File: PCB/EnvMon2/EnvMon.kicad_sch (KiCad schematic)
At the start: 40 parts, among them J1 USB-C, J2 DC, J3 TEMP, J4 Shelly, M1 OLED1.5-RGB, SW1 SW_Push, SW2 SW_Push, SW3 SW_Push, U1 LMR16006XDDCR, U2 SCD41, U3 FT231XQ, U4 ESP32-PICO-MINI-02, U5 QR, U7 SHT40, U8 VEML6040

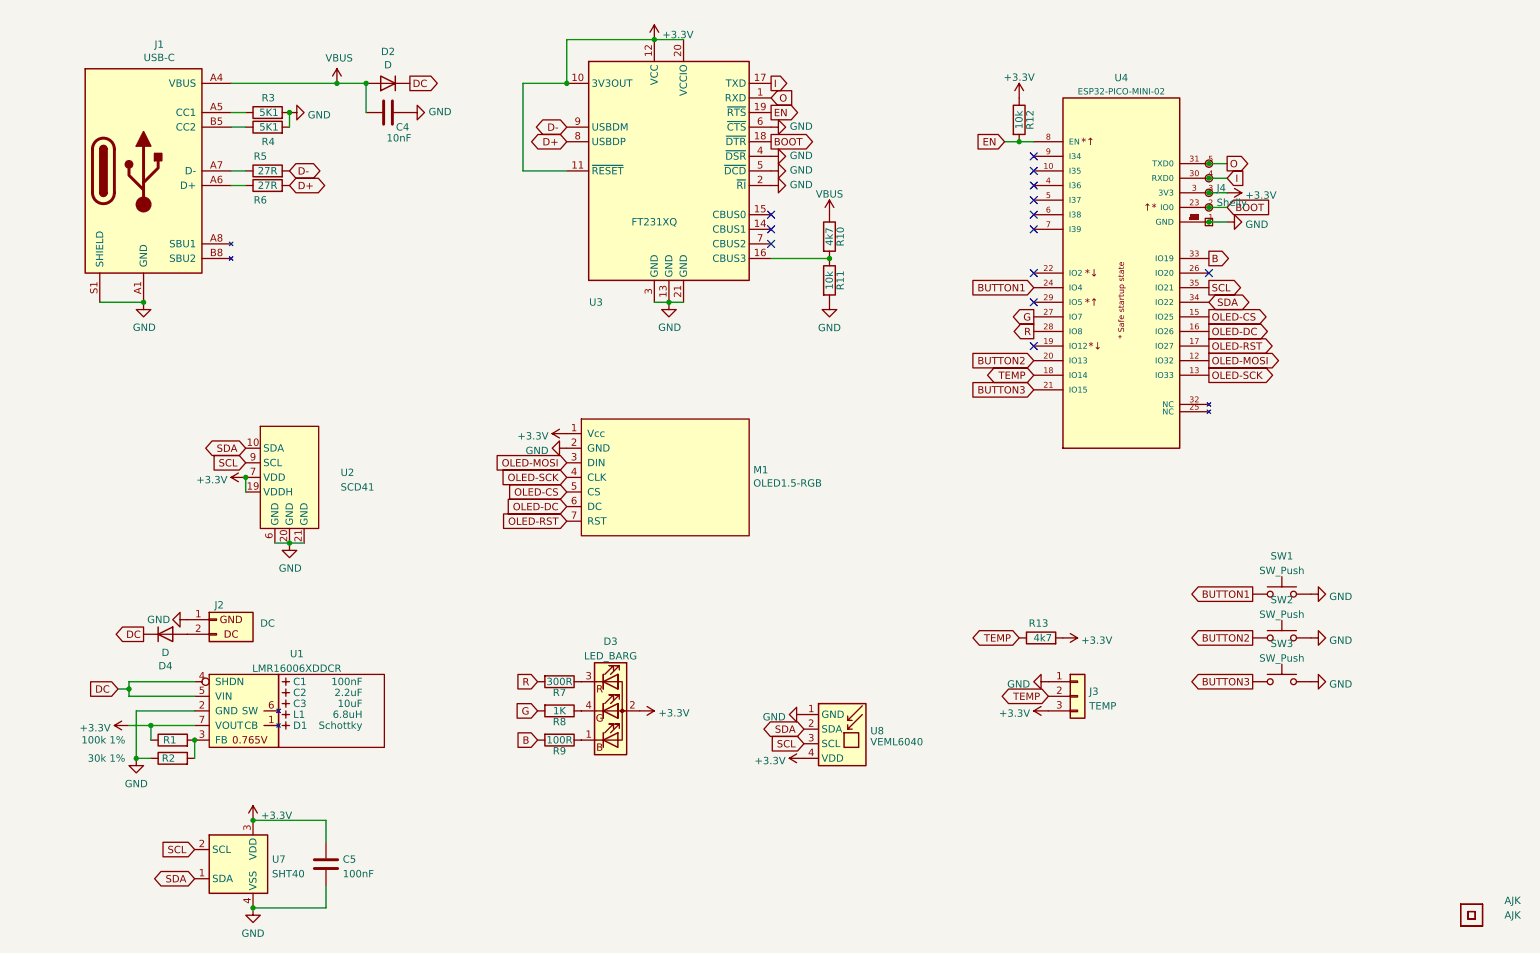
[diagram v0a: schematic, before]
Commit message: S3 board basic tracking started
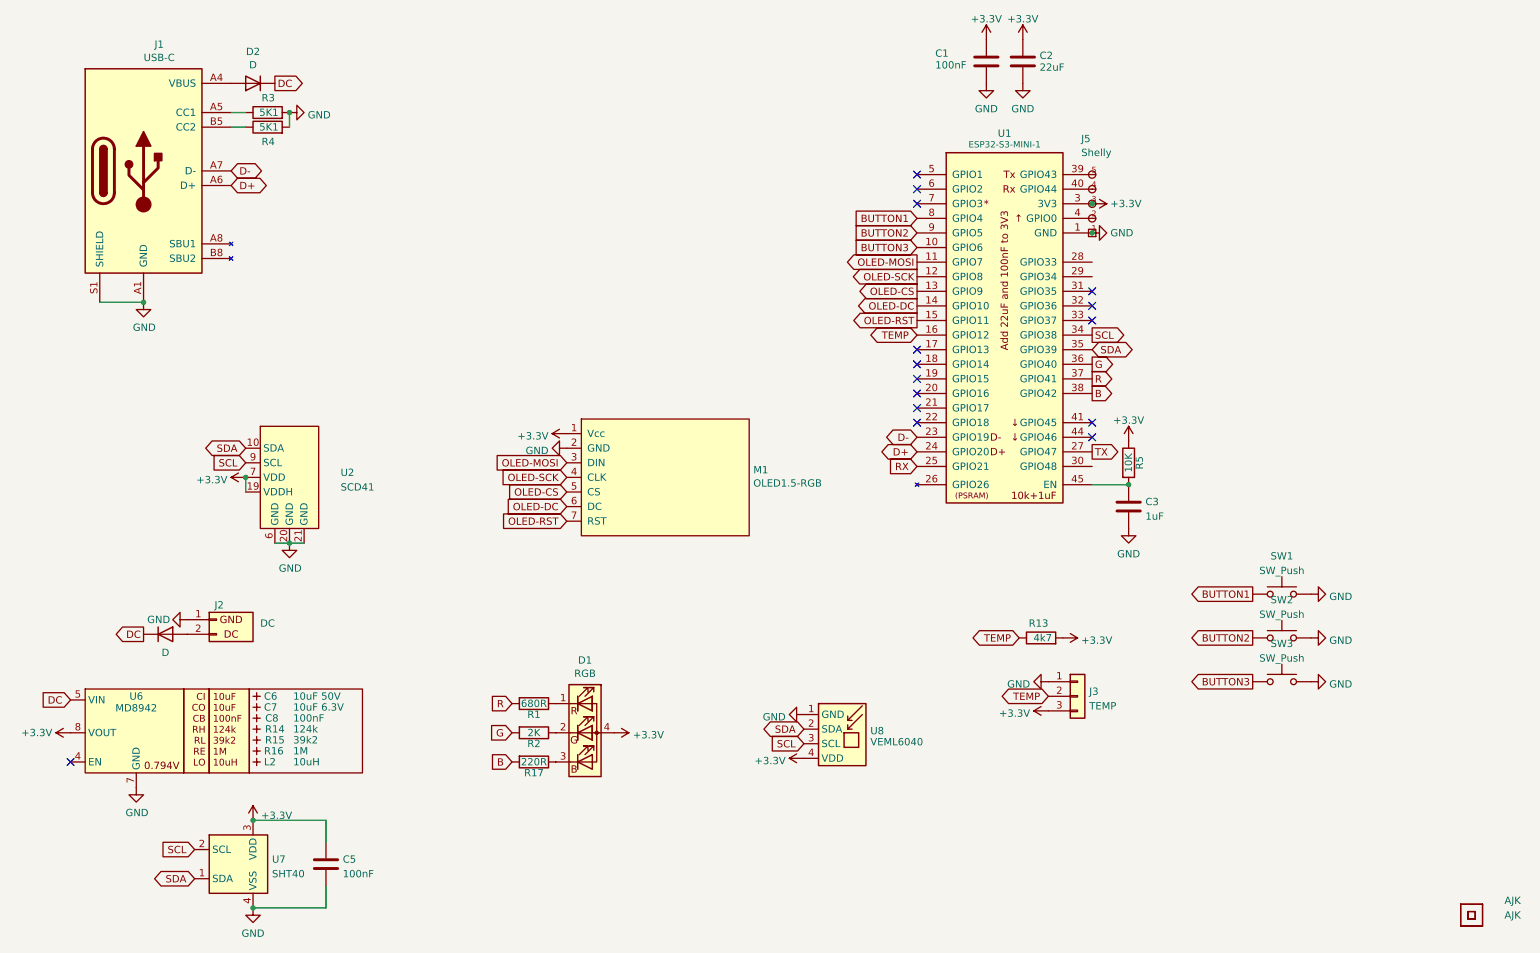
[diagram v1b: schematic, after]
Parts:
- removed C1: 100nF, RevK:C_0603_, symbol RevK:Hidden
- removed C2: 2.2uF, RevK:C_0805_, symbol RevK:Hidden
- removed C3: 10uF, RevK:C_0805_, symbol RevK:Hidden
- removed C4: 10nF, RevK:C_0603, symbol Device:C
- removed D1: Schottky, RevK:D_1206_, symbol RevK:Hidden
- removed D3: LED_BARG, RevK:MHS190RGBCT, symbol Device:LED_BARG
- removed J4: Shelly, RevK:Shelly, symbol RevK:Shelly
- removed L1: 6.8uH, RevK:L_4x4_, symbol RevK:Hidden
- removed R10: 4k7, RevK:R_0603, symbol Device:R
- removed R11, R12: 10k, RevK:R_0603, symbol Device:R
- removed R6: 27R, RevK:R_0603, symbol Device:R
- removed R7: 300R, RevK:R_0603, symbol Device:R
- removed R8: 1K, RevK:R_0603, symbol Device:R
- removed R9: 100R, RevK:R_0603, symbol Device:R
- removed U1: LMR16006XDDCR, RevK:SOT-23-Thin-6-Reg, symbol RevK:LMR16006XDDCR
- removed U3: FT231XQ, RevK:QFN-20-1EP_4x4mm_P0.5mm_EP2.5x2.5mm, symbol RevK:FT231XQ
- removed U4: ESP32-PICO-MINI-02, RevK:ESP32-PICO-MINI-02, symbol RevK:ESP32-PICO-MINI-02
- added C1: 100nF, RevK:C_0402, symbol Device:C
- added C2: 22uF, RevK:C_0402, symbol Device:C
- added C3: 1uF, RevK:C_0402, symbol Device:C
- added C6: 10uF 50V, RevK:C_0603_, symbol RevK:Hidden
- added C7: 10uF 6.3V, RevK:C_0603_, symbol RevK:Hidden
- added C8: 100nF, RevK:C_0603_, symbol RevK:Hidden
- added D1: RGB, RevK:LED-RGB-1.6x1.6, symbol Device:LED_RGBA
- added J5: Shelly, RevK:Shelly, symbol RevK:Shelly
- added L2: 10uH, RevK:L_4x4_, symbol RevK:Hidden
- added R14: 124k, RevK:R_0402_, symbol RevK:Hidden
- added R15: 39k2, RevK:R_0402_, symbol RevK:Hidden
- added R16: 1M, RevK:R_0402_, symbol RevK:Hidden
- added R17: 220R, RevK:R_0402, symbol Device:R
- added U1: ESP32-S3-MINI-1, RevK:ESP32-S3-MINI-1, symbol RevK:ESP32-S3-MINI-1-N4R2
- added U6: MD8942, RevK:SOT-23-6-MD8942, symbol RevK:MD89420-RegBlock
- C5: footprint RevK:C_0603 -> RevK:C_0402
- R1: value 100k 1% -> 680R; footprint RevK:R_0603 -> RevK:R_0402; LCSC Part # C14675 -> (none)
- R13, R3, R4: footprint RevK:R_0603 -> RevK:R_0402
- R2: value 30k 1% -> 2K; footprint RevK:R_0603 -> RevK:R_0402; LCSC Part # C100001 -> (none)
- R5: value 27R -> 10K; footprint RevK:R_0603 -> RevK:R_0402
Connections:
- net +3.3V: now also R5.1, C1.1, C2.1, D1.4 (A), J5.3 (3V3), U1.3 (3V3), U6.8 (VOUT); no longer R1.1
- net B: now also R17.2, U1.38 (GPIO42)
- net BUTTON1: now also U1.8 (GPIO4)
- net BUTTON2: now also U1.9 (GPIO5)
- net BUTTON3: now also U1.10 (GPIO6)
- net D+: now also J1.A6 (D+), J1.B6 (D+), U1.24 (GPIO20)
- net D-: now also J1.A7 (D-), J1.B7 (D-), U1.23 (GPIO19); no longer R5.2
- net DC: now also U6.5 (VIN)
- net G: now also R2.2, U1.36 (GPIO40)
- net GND: now also C1.2, C2.2, C3.2, J5.1 (GND), U1.1 (GND), U1.2 (GND), U1.42 (GND), U1.43 (GND), U1.46 (GND), U1.47 (GND), U1.48 (GND), U1.49 (GND), U1.50 (GND), U1.51 (GND), U1.52 (GND), U1.53 (GND), U1.54 (GND), U1.55 (GND), U1.56 (GND), U1.57 (GND), U1.58 (GND), U1.59 (GND), U1.60 (GND), U1.61 (GND), U1.62 (GND), U1.63 (GND), U1.64 (GND), U1.65 (GND), U6.2 (GND), U6.7 (GND); no longer R2.1
- net OLED-CS: now also U1.13 (GPIO9)
- net OLED-DC: now also U1.14 (GPIO10)
- net OLED-MOSI: now also U1.11 (GPIO7)
- net OLED-RST: now also U1.15 (GPIO11)
- net OLED-SCK: now also U1.12 (GPIO8)
- net R: now also R1.2, U1.37 (GPIO41)
- net SCL: now also U1.34 (GPIO38)
- net SDA: now also U1.35 (GPIO39)
- net TEMP: now also U1.16 (GPIO12)
- net VBUS: no longer names the net of D2.2 (A), J1.A4 (VBUS), J1.A9 (VBUS), J1.B4 (VBUS), J1.B9 (VBUS)
- new net: J5.2 (0), U1.4 (GPIO0)
- new net: J5.4 (Rx), U1.40 (GPIO44)
- new net: J5.5 (Tx), U1.39 (GPIO43)
- new net: D1.2 (GK), R2.1
- new net: C3.1, R5.2, U1.45 (EN)
- new net: D1.1 (RK), R1.1
- new net: D1.3 (BK), R17.1
- new net RX: U1.25 (GPIO21)
- new net TX: U1.27 (GPIO47)
- no-connect marks 13 -> 15
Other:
- moved on the sheet: D2

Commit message: Pretty tracks
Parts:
- removed D4: D, RevK:D_1206, symbol Device:D
- added D3: D, RevK:D_SOD-123, symbol Device:D
- D2: footprint RevK:D_1206 -> RevK:D_SOD-123; LCSC Part # C143805 -> C1884542
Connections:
- net DC: now also D3.1 (K)
- net at J1.A4 (VBUS), J1.A9 (VBUS), J1.B4 (VBUS)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: now also D3.2 (A); no longer D2.2 (A)
- net at J2.2 (DC): now also D2.2 (A)
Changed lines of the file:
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@@
+    )
+  )
+  (symbol (lib_id "Device:D") (at 44.45 123.825 0) (unit 1)
+    (in_bom yes) (on_board yes) (dnp no)
+    (property "Reference" "D2" (at 44.45 129.3368 0)
+      (effects (font (size 1.27 1.27)))
+    )
+    (property "Value" "D" (at 44.45 127.0254 0)
+      (effects (font (size 1.27 1.27)))
+    )
+    (property "Footprint" "RevK:D_SOD-123" (at 44.45 123.825 0)
+      (effects (font (size 1.27 1.27)) hide)
+    )
+    (property "Datasheet" "~" (at 44.45 123.825 0)
+      (effects (font (size 1.27 1.27)) hide)
+    )
+    (property "LCSC Part #" "C1884542" (at 44.45 123.825 0)
+      (effects (font (size 1.27 1.27)) hide)
+    )
+    (pin "1")
+    (pin "2")
+    (instances
+      (project "EnvMon"
+        (path "/12422a89-3d0c-485c-9386-f77121fd68fd"
+          (reference "D2") (unit 1)
+        )
+      )
+      (project "Access"
+        (path "/2a267270-6585-45e3-a633-b53049f10066"
+          (reference "D8") (unit 1)
+        )
+      )
+      (project "GenericS3"
+        (path "/2d210a96-f81f-42a9-8bf4-1b43c11086f3"
+          (reference "D1") (unit 1)
+        )
+      )
     )
   )
@@
     )
   )
-  (symbol (lib_id "Device:D") (at 44.45 123.825 0) (unit 1)
-    (in_bom yes) (on_board yes) (dnp no)
-    (property "Reference" "D4" (at 44.45 129.3368 0)
-      (effects (font (size 1.27 1.27)) hide)
-    )
-    (property "Value" "D" (at 44.45 127.0254 0)
-      (effects (font (size 1.27 1.27)))
-    )
-    (property "Footprint" "RevK:D_1206" (at 44.45 123.825 0)
-      (effects (font (size 1.27 1.27)) hide)
-    )
-    (property "Datasheet" "~" (at 44.45 123.825 0)
-      (effects (font (size 1.27 1.27)) hide)
-    )
-    (property "LCSC Part #" "C143805" (at 44.45 123.825 0)
-      (effects (font (size 1.27 1.27)) hide)
-    )
-    (pin "1")
-    (pin "2")
-    (instances
-      (project "EnvMon"
-        (path "/12422a89-3d0c-485c-9386-f77121fd68fd"
-          (reference "D4") (unit 1)
-        )
-      )
-    )
-  )
   (symbol (lib_id "Device:R") (at 196.85 124.46 90) (unit 1)
     (in_bom yes) (on_board yes) (dnp no)
@@
         (path "/12422a89-3d0c-485c-9386-f77121fd68fd"
           (reference "U5") (unit 1)
+        )
+      )
+    )
+  )
+  (symbol (lib_id "Device:D") (at 59.69 27.94 180) (unit 1)
+    (in_bom yes) (on_board yes) (dnp no)
+    (property "Reference" "D3" (at 59.69 22.4282 0)
+      (effects (font (size 1.27 1.27)))
+    )
+    (property "Value" "D" (at 59.69 24.7396 0)
+      (effects (font (size 1.27 1.27)))
+    )
+    (property "Footprint" "RevK:D_SOD-123" (at 59.69 27.94 0)
+      (effects (font (size 1.27 1.27)) hide)
+    )
+    (property "Datasheet" "~" (at 59.69 27.94 0)
+      (effects (font (size 1.27 1.27)) hide)
+    )
+    (property "LCSC Part #" "C1884542" (at 59.69 27.94 0)
+      (effects (font (size 1.27 1.27)) hide)
+    )
+    (pin "1")
+    (pin "2")
+    (instances
+      (project "EnvMon"
+        (path "/12422a89-3d0c-485c-9386-f77121fd68fd"
+          (reference "D3") (unit 1)
+        )
+      )
+      (project "Access"
+        (path "/2a267270-6585-45e3-a633-b53049f10066"
+          (reference "D8") (unit 1)
+        )
+      )
+      (project "GenericS3"
+        (path "/2d210a96-f81f-42a9-8bf4-1b43c11086f3"
+          (reference "D1") (unit 1)
         )
       )
@@
         )
       )
-    )
-  )
-  (symbol (lib_id "Device:D") (at 59.69 27.94 180) (unit 1)
-    (in_bom yes) (on_board yes) (dnp no)
-    (property "Reference" "D2" (at 59.69 22.4282 0)
-      (effects (font (size 1.27 1.27)))
-    )
-    (property "Value" "D" (at 59.69 24.7396 0)
-      (effects (font (size 1.27 1.27)))
-    )
-    (property "Footprint" "RevK:D_1206" (at 59.69 27.94 0)
-      (effects (font (size 1.27 1.27)) hide)
-    )
-    (property "Datasheet" "~" (at 59.69 27.94 0)
-      (effects (font (size 1.27 1.27)) hide)
-    )
-    (property "LCSC Part #" "C143805" (at 59.69 27.94 0)
-      (effects (font (size 1.27 1.27)) hide)
-    )
-    (pin "1")
-    (pin "2")
-    (instances
-      (project "EnvMon"
-        (path "/12422a89-3d0c-485c-9386-f77121fd68fd"
-          (reference "D2") (unit 1)
-        )
-      )
